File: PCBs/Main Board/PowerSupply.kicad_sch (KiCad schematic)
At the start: 2 parts, among them J9 S2P-VHLFSN, U4 173010378

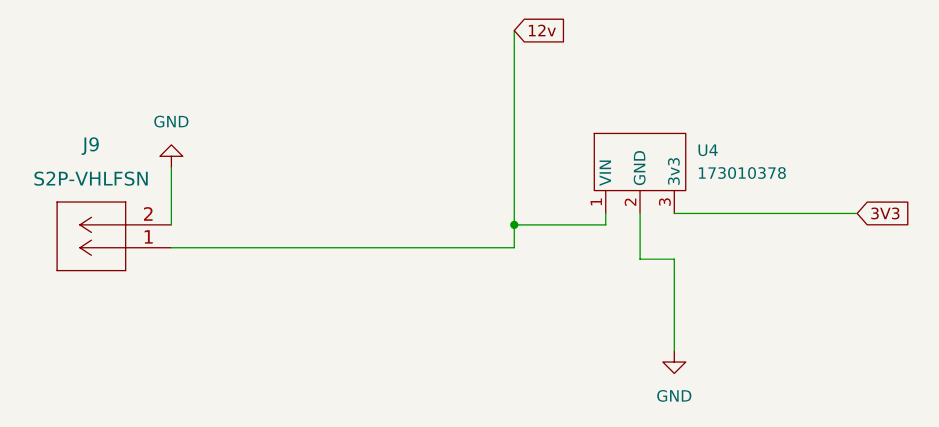
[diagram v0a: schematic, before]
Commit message: Remove steppers, add OLED
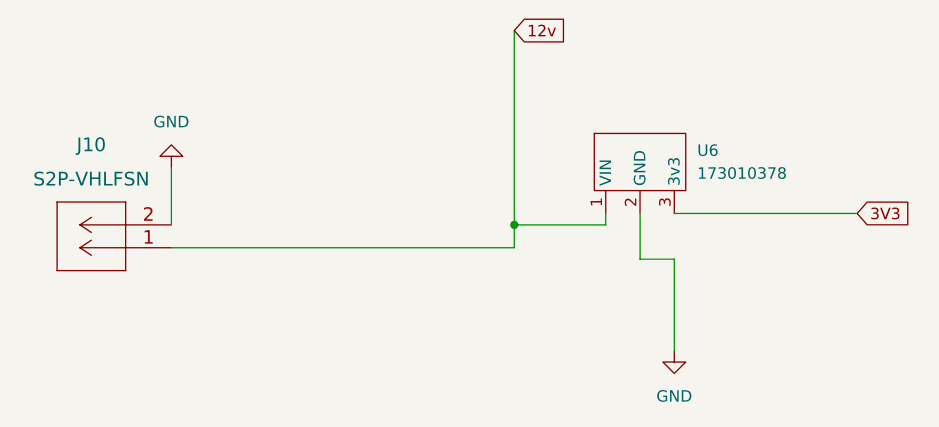
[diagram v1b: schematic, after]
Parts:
- renumbered J9 to J10, U4 to U6
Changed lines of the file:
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@@
   (symbol (lib_id "power:GND") (at 50.8 76.2 180) (unit 1)
     (in_bom yes) (on_board yes) (fields_autoplaced)
-    (property "Reference" "#PWR012" (id 0) (at 50.8 69.85 0)
+    (property "Reference" "#PWR020" (id 0) (at 50.8 69.85 0)
       (effects (font (size 1.27 1.27)) hide)
     )
@@
   (symbol (lib_id "power:GND") (at 106.68 96.52 0) (unit 1)
     (in_bom yes) (on_board yes) (fields_autoplaced)
-    (property "Reference" "#PWR013" (id 0) (at 106.68 102.87 0)
+    (property "Reference" "#PWR021" (id 0) (at 106.68 102.87 0)
       (effects (font (size 1.27 1.27)) hide)
     )
@@
   (symbol (lib_id "Hydro_Library:173010378") (at 97.79 72.39 0) (unit 1)
     (in_bom yes) (on_board yes) (fields_autoplaced)
-    (property "Reference" "U4" (id 0) (at 109.22 74.2949 0)
+    (property "Reference" "U6" (id 0) (at 109.22 74.2949 0)
       (effects (font (size 1.27 1.27)) (justify left))
     )
@@
   (symbol (lib_id "S2P-VH(LF)(SN):S2P-VHLFSN") (at 50.8 85.09 180) (unit 1)
     (in_bom yes) (on_board yes) (fields_autoplaced)
-    (property "Reference" "J9" (id 0) (at 41.91 73.66 0)
+    (property "Reference" "J10" (id 0) (at 41.91 73.66 0)
       (effects (font (size 1.524 1.524)))
     )

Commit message: Changed some pins
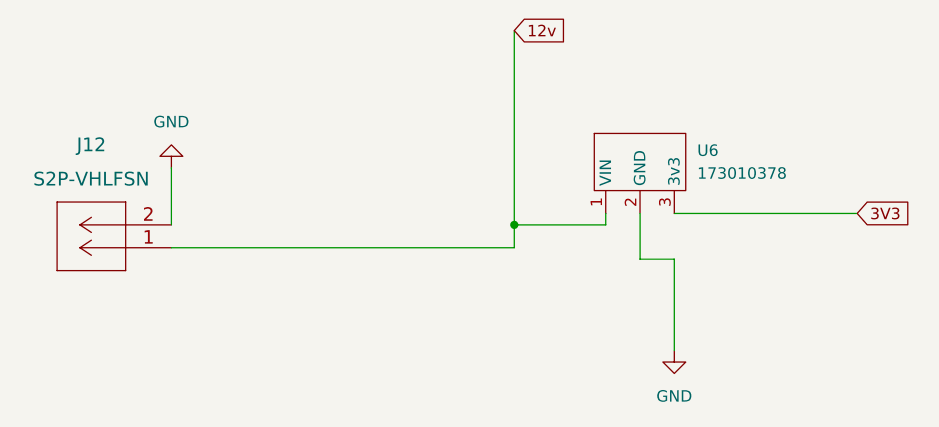
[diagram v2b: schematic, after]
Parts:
- renumbered J10 to J12
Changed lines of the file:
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@@
   (symbol (lib_id "power:GND") (at 50.8 76.2 180) (unit 1)
     (in_bom yes) (on_board yes) (fields_autoplaced)
-    (property "Reference" "#PWR020" (id 0) (at 50.8 69.85 0)
+    (property "Reference" "#PWR023" (id 0) (at 50.8 69.85 0)
       (effects (font (size 1.27 1.27)) hide)
     )
@@
   (symbol (lib_id "power:GND") (at 106.68 96.52 0) (unit 1)
     (in_bom yes) (on_board yes) (fields_autoplaced)
-    (property "Reference" "#PWR021" (id 0) (at 106.68 102.87 0)
+    (property "Reference" "#PWR024" (id 0) (at 106.68 102.87 0)
       (effects (font (size 1.27 1.27)) hide)
     )
@@
   (symbol (lib_id "S2P-VH(LF)(SN):S2P-VHLFSN") (at 50.8 85.09 180) (unit 1)
     (in_bom yes) (on_board yes) (fields_autoplaced)
-    (property "Reference" "J10" (id 0) (at 41.91 73.66 0)
+    (property "Reference" "J12" (id 0) (at 41.91 73.66 0)
       (effects (font (size 1.524 1.524)))
     )
